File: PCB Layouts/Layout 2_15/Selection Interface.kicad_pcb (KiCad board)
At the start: 4 copper layers, 110 x 90 mm, 132 parts, among them P1 CONN_01X02, P11 CONN_01X02, P12 CONN_01X02, P13 CONN_01X10, P14 CONN_01X02, P15 CONN_01X02, P16 CONN_01X02, P18 CONN_02X05, P2 CONN_01X02, P3 CONN_01X02, P4 CONN_01X02, P5 CONN_01X02, P6 CONN_02X10, P7 CONN_01X02, P8 CONN_02X04, P9 CONN_01X02

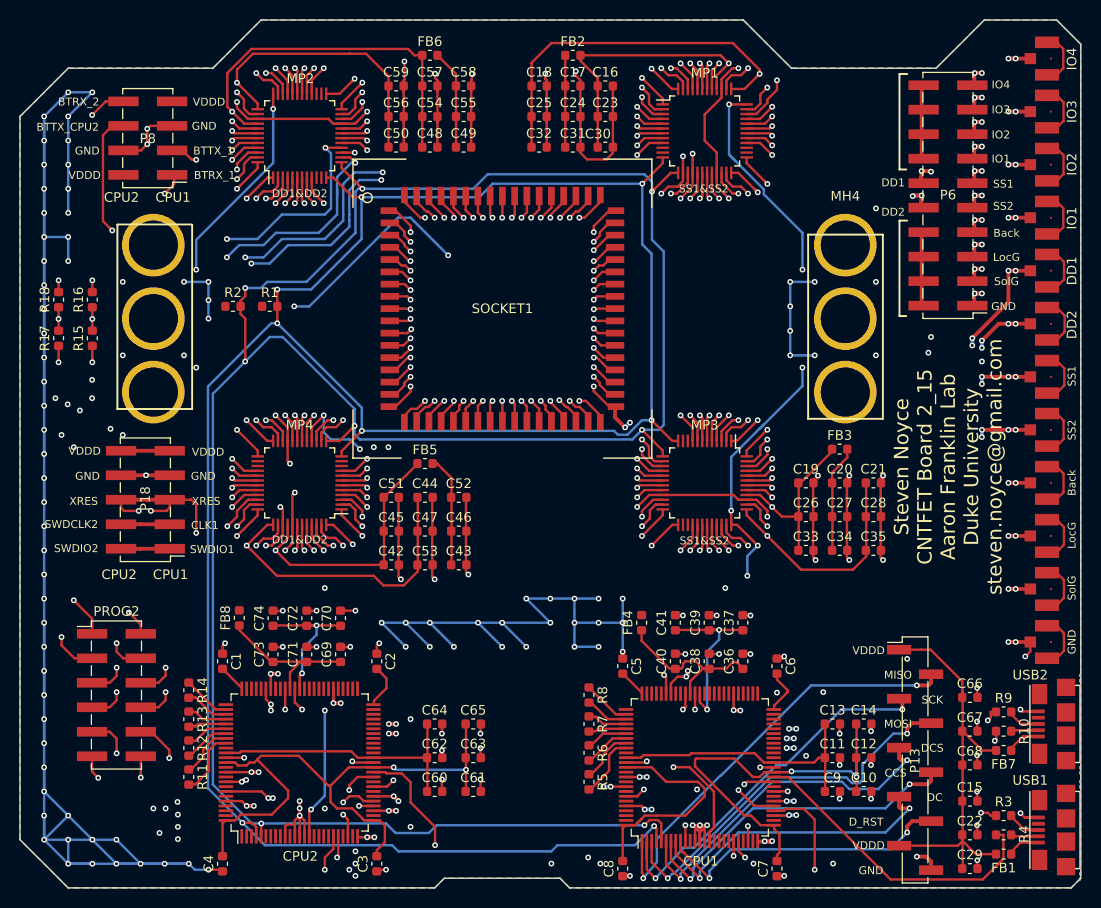
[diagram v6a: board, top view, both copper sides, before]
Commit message: Finished routing programming signals for layout 2_15
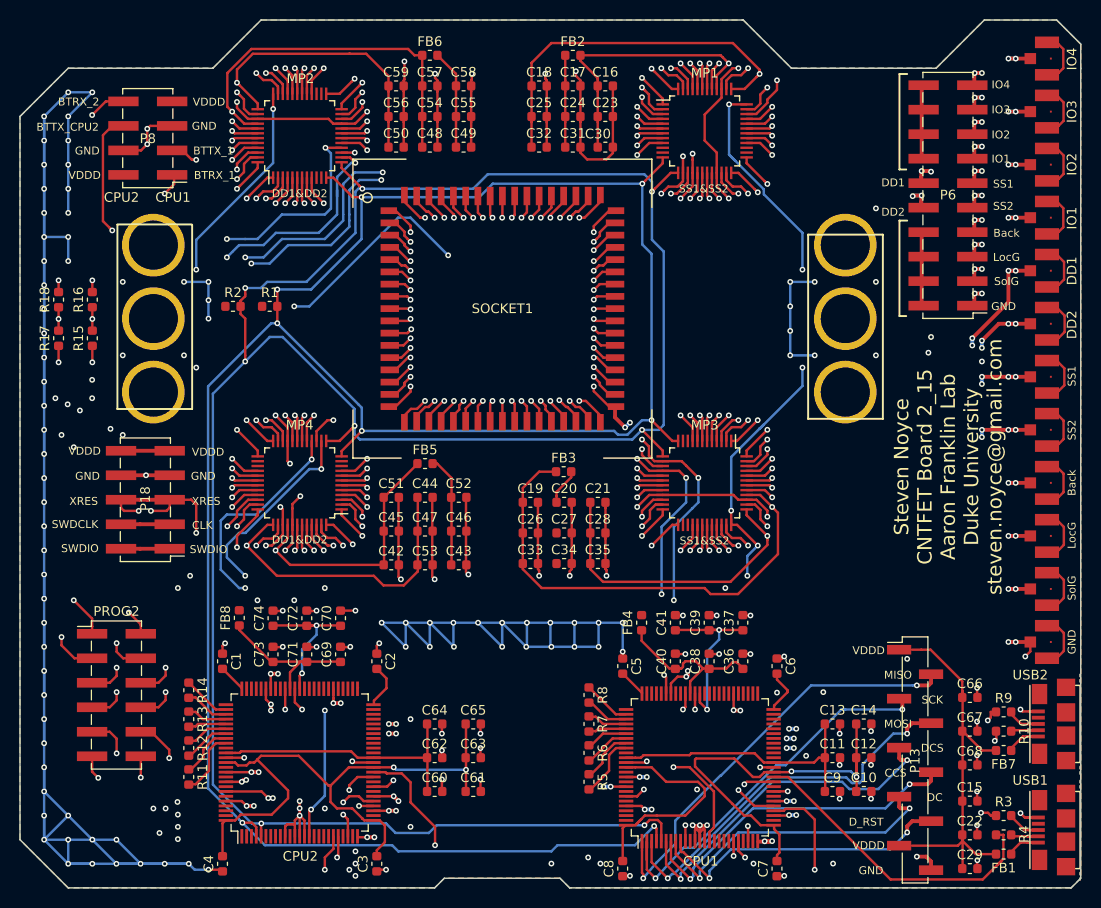
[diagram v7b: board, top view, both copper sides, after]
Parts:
- moved FB3 28.7 mm to (206.4, 116.8)
- moved C19 28.6 mm to (202.9, 120.0)
- moved C20 28.6 mm to (206.4, 120.0)
- moved C21 28.6 mm to (209.9, 120.0)
- moved C26 28.6 mm to (202.9, 123.2)
- moved C27 28.6 mm to (206.4, 123.2)
- moved C28 28.6 mm to (209.9, 123.2)
- moved C33 28.6 mm to (202.9, 126.4)
- moved C34 28.6 mm to (206.4, 126.4)
- moved C35 28.6 mm to (209.9, 126.4)
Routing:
- net D49: track 40.2 -> 103.8 mm, vias 4 -> 6
- net D50: track 41.2 -> 104.2 mm, vias 4 -> 6
- net SWDIO4: track 7.36 -> 42.5 mm, vias 2 -> 4
- net SWDCLK4: track 13.1 -> 46.6 mm, vias 3 -> 4
- net Net-(C19-Pad1): track 18.4 -> 50.1 mm
- net Net-(C21-Pad1): track 23.5 -> 32.0 mm
- net VDDD: track 313.5 -> 306.2 mm
- net GND: track 557.1 -> 562.0 mm, vias 183 -> 178
- net XRES: track 250.6 -> 251.4 mm
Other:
- board text added: "CLK"
- board text added: "SWDCLK"
- board text added: "SWDIO"
- board text removed: "CLK1"
- board text removed: "SWDCLK2"
- board text removed: "SWDIO1"
- board text removed: "SWDIO2"

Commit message: Adding finishing touches (I think) to Layout 2_15. The main thing left to do is to look into making more devices accessible for the multiplexers since some of the pins on the current version are restricted
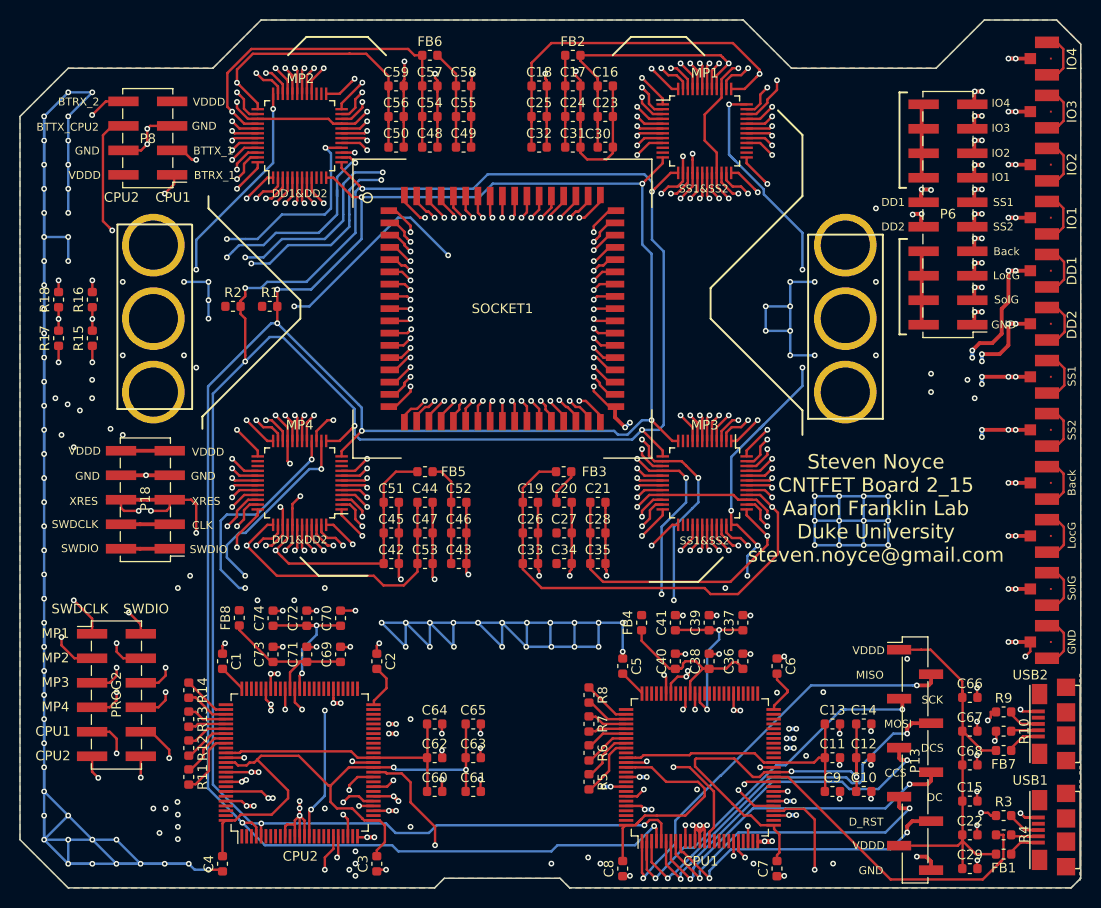
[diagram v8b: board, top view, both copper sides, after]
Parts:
- moved P6 1.98 mm to (246.2, 90.2)
- moved FB5 0.84 mm to (192.0, 116.8)
- moved C44 0.52 mm to (192.0, 120.0)
- moved C51 0.52 mm to (188.5, 120.0)
- moved C52 0.52 mm to (195.5, 120.0)
- moved C45 0.19 mm to (188.5, 123.2)
- moved C46 0.19 mm to (195.5, 123.2)
- moved C47 0.19 mm to (192.0, 123.2)
- moved C42 0.14 mm to (188.5, 126.4)
- moved C43 0.14 mm to (195.5, 126.4)
- moved C53 0.14 mm to (192.0, 126.4)
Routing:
- net GND: track 562.0 -> 611.2 mm, vias 178 -> 192
- net IO2: track 136.1 -> 131.5 mm
- net IO1: track 147.3 -> 143.3 mm
- net LocalGates: track 179.8 -> 177.1 mm
- net DD1: track 287.8 -> 290.2 mm, vias 17 -> 18
- net BackGate: track 175.3 -> 173.4 mm
- net DD2: track 280.9 -> 282.5 mm
- net SolutionGate: track 182.4 -> 181.1 mm
- net SS1: track 206.4 -> 205.3 mm
- net SS2: track 203.1 -> 202.0 mm
- net IO3: track 143.1 -> 142.1 mm
- net VDDD: track 306.2 -> 305.4 mm
- net IO4: track 143.0 -> 142.3 mm
- net Net-(C44-Pad1): track 31.4 -> 30.9 mm
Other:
- board text added: "MP1"
- board text added: "MP2"
- board text added: "MP3"
- board text added: "MP4"
